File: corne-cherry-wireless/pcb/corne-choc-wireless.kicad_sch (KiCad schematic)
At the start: 96 parts, among them J2 Nice!View, J4 Nice!View, SW1 SW_PUSH, SW10 SW_PUSH, SW11 SW_PUSH, SW12 SW_PUSH, SW13 SW_PUSH, SW14 SW_PUSH, SW15 SW_PUSH, SW16 SW_PUSH, SW17 SW_PUSH, SW18 SW_PUSH, SW19 SW_PUSH, SW2 SW_PUSH, SW20 SW_PUSH, SW21 SW_PUSH, SW22 SW_PUSH, SW23 SW_PUSH, SW24 SW_PUSH, SW25 SW_PUSH, SW26 SW_PUSH, SW27 SW_PUSH, SW29 SW_PUSH, SW3 SW_PUSH, SW30 SW_PUSH, SW31 SW_PUSH, SW32 SW_PUSH, SW33 SW_PUSH, SW34 SW_PUSH, SW35 SW_PUSH, SW36 SW_PUSH, SW37 SW_PUSH, SW38 SW_PUSH, SW39 SW_PUSH, SW4 SW_PUSH, SW40 SW_PUSH, SW41 SW_PUSH, SW42 SW_PUSH, SW5 SW_PUSH, SW6 SW_PUSH, SW8 SW_PUSH, SW9 SW_PUSH, U1 Nice!Nano, U2 Nice!Nano

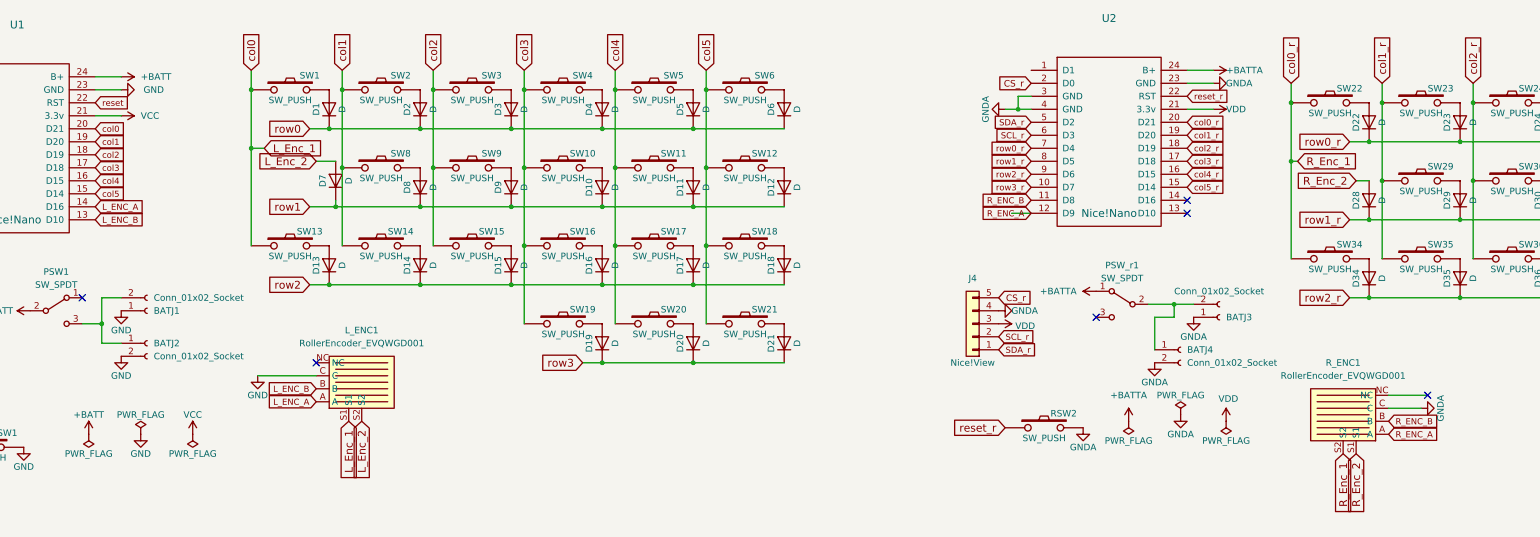
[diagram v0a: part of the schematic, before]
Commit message: Add submodules
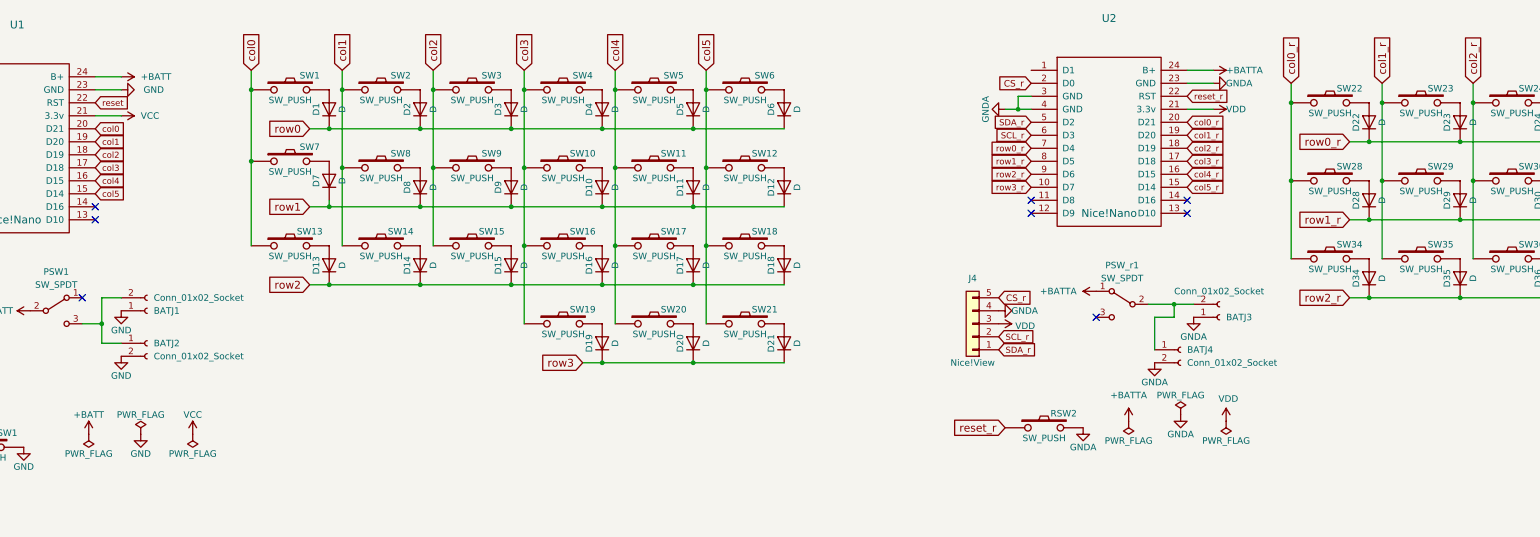
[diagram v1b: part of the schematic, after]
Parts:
- removed L_ENC1, R_ENC1: RollerEncoder_EVQWGD001, zzkeeb:RotaryEncoder_EVQWGD001, symbol zzkeebs:RollerEncoder_EVQWGD001
- added SW28, SW7: SW_PUSH, kbd:CherryMX_Hotswap, symbol kbd:SW_PUSH
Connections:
- net L_ENC_A: no longer names the net of U1.14 (D16)
- net L_ENC_B: no longer names the net of U1.13 (D10)
- net L_Enc_1 renamed col0
- net col0: now also SW7.1
- net L_Enc_2: no longer names the net of D7.2 (A)
- net L_Enc_2: now also SW7.2
- net R_ENC_A: no longer names the net of U2.12 (D9)
- net R_ENC_B: no longer names the net of U2.11 (D8)
- net R_Enc_1 renamed col0_r
- net col0_r: now also SW28.1
- net R_Enc_2: no longer names the net of D28.2 (A)
- net R_Enc_2: now also SW28.2
- no-connect marks 8 -> 10
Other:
- moved on the sheet: D7
